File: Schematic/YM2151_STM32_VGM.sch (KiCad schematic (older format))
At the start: 32 parts, among them J1 Jack_DC+12V, J1 Micro_SD_Card, J2 USB_B, U1 BluePill_STM32F103C, U2 LTC6903, U3 LD1117, U4 LM2596S-5.0, U5 CH340G, U6 OLED_128x32_I2C, U7 YM2151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

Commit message: Schematic complete
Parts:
- added 1uF: C17, symbol CP1_Small
- added 1uF: C18, symbol CP1_Small
- added C15, C16: 1uF, symbol CP1_Small
- added C19, C20: 0.22uF, symbol C_Small
- added C21, C22: 68nF, symbol C_Small
- added C23, C24: 1000uF, symbol CP1_Small
- added J3: JACK_TRS_6PINS, symbol JACK_TRS_6PINS
- added L2, L3: 22uH, symbol L
- added SW1: PWR_SWITCH, symbol SW_SPST
- added SW2: MUTE_SWITCH, symbol SW_SPDT
- added SW3: PREV, symbol SW_Push_Dual
- added SW4: RAND, symbol SW_Push_Dual
- added SW5: NEXT, symbol SW_Push_Dual
- added SW6: LOOP, symbol SW_Push_Dual
- added SW7: SHUF, symbol SW_Push_Dual
- added U10: TPA3122D2, symbol TPA3122D2
- renumbered J1 to J2
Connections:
- net labels added: LEFT_OP_OUT, LOOP, L_OUT, NEXT, PREV, RAND, RIGHT_OP_OUT, R_OUT, SHUF
- net labels removed: LEFT_AUDIO_OUT, RIGHT_AUDIO_OUT
- wire segments 113 -> 164
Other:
- note added: "External 3.3v reg. to reduce noise from OLED+SD card\n"

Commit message: In progress of appending footprints
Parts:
- removed J1: Micro_SD_Card, symbol Micro_SD_Card
- added J1: DM3CS-SF (Micro SD Card Slot), Connector_Card:SD_TE_2041021, symbol DM3CS-SF
- D1: value 1N5824 -> SS34; footprint (none) -> Diodes:DO-214AB
- J2: footprint (none) -> Connectors:BARREL_JACK
- J3: footprint (none) -> Connectors:PJ320E_3.5mm_Jack
- J4: renamed from J2; footprint (none) -> Connectors:USB_B
- SW1, SW2: footprint (none) -> Switches:1825115-1
- SW3, SW4, SW5, SW6, SW7: footprint (none) -> Buttons_Switches_THT:SW_TH_Tactile_Omron_B3F-10xx
- U10: footprint (none) -> Housings_DIP:DIP-20_W7.62mm
- U2: footprint (none) -> Housings_SSOP:MSOP-8_3x3mm_Pitch0.65mm
- U3: footprint TO_SOT_Packages_SMD:SOT-223-3Lead_TabPin2 -> TO_SOT_Packages_THT:TO-220-3_Horizontal
- U6: footprint (none) -> CustomDisplays:128x32_OLED_I2C_Module
- U7: footprint (none) -> Housings_DIP:DIP-24_W15.24mm
- U8: footprint (none) -> Housings_DIP:DIP-16_W7.62mm
- U9: footprint (none) -> Housings_DIP:DIP-14_W7.62mm
- Y1: footprint (none) -> Crystals:Crystal_HC49-U_Vertical
- gave numbers to parts that had none: 1
- renumbered 100nF to 100nF1, 1uF to 1uF1, 1uF to 1uF2, C13 to C25
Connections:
- wire segments 164 -> 165

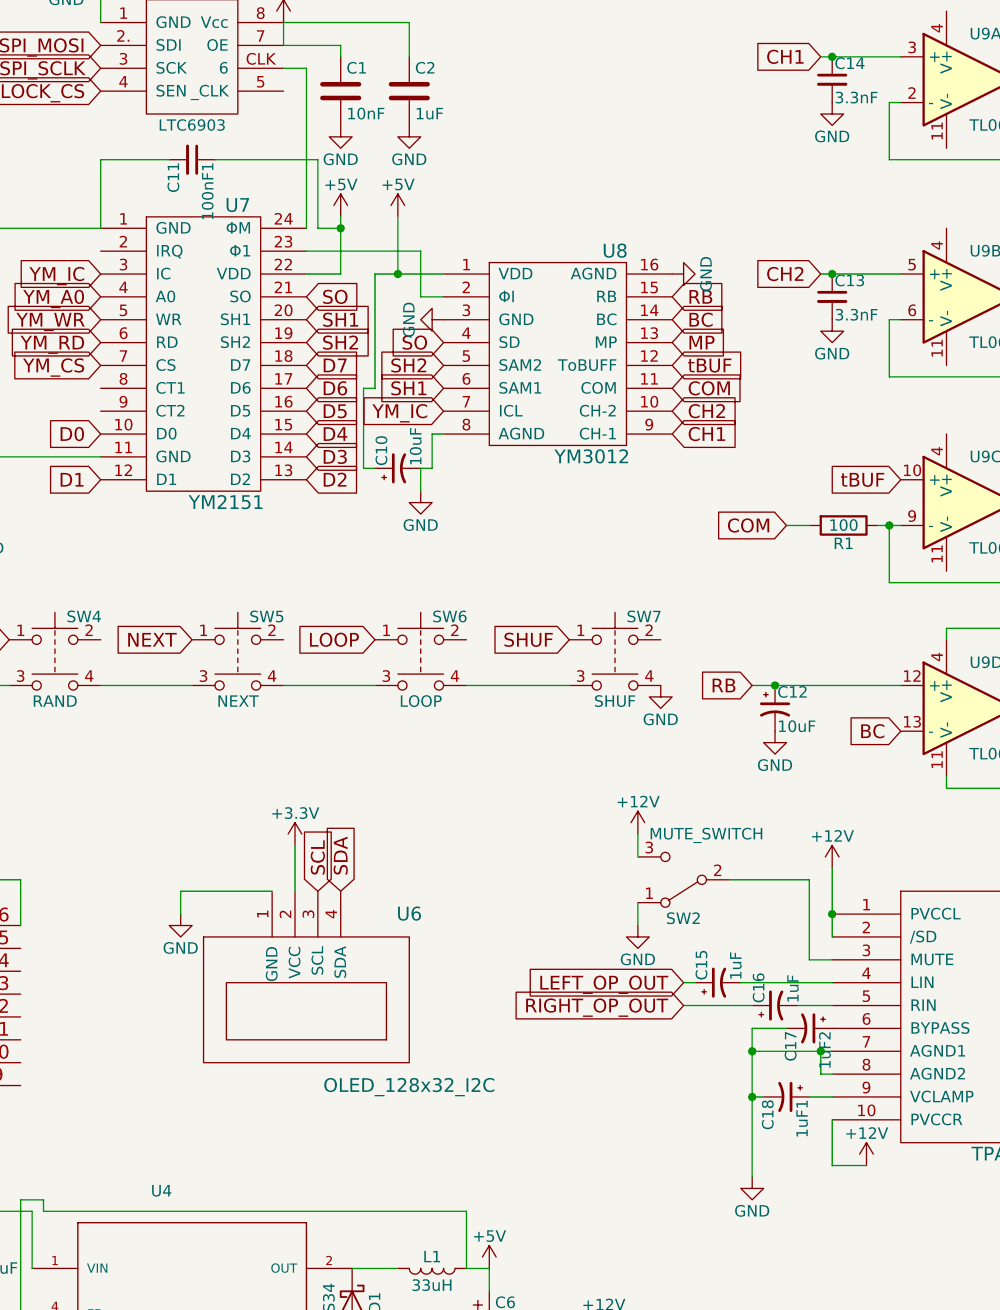
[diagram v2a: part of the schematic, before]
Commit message: Footprint selection finalized
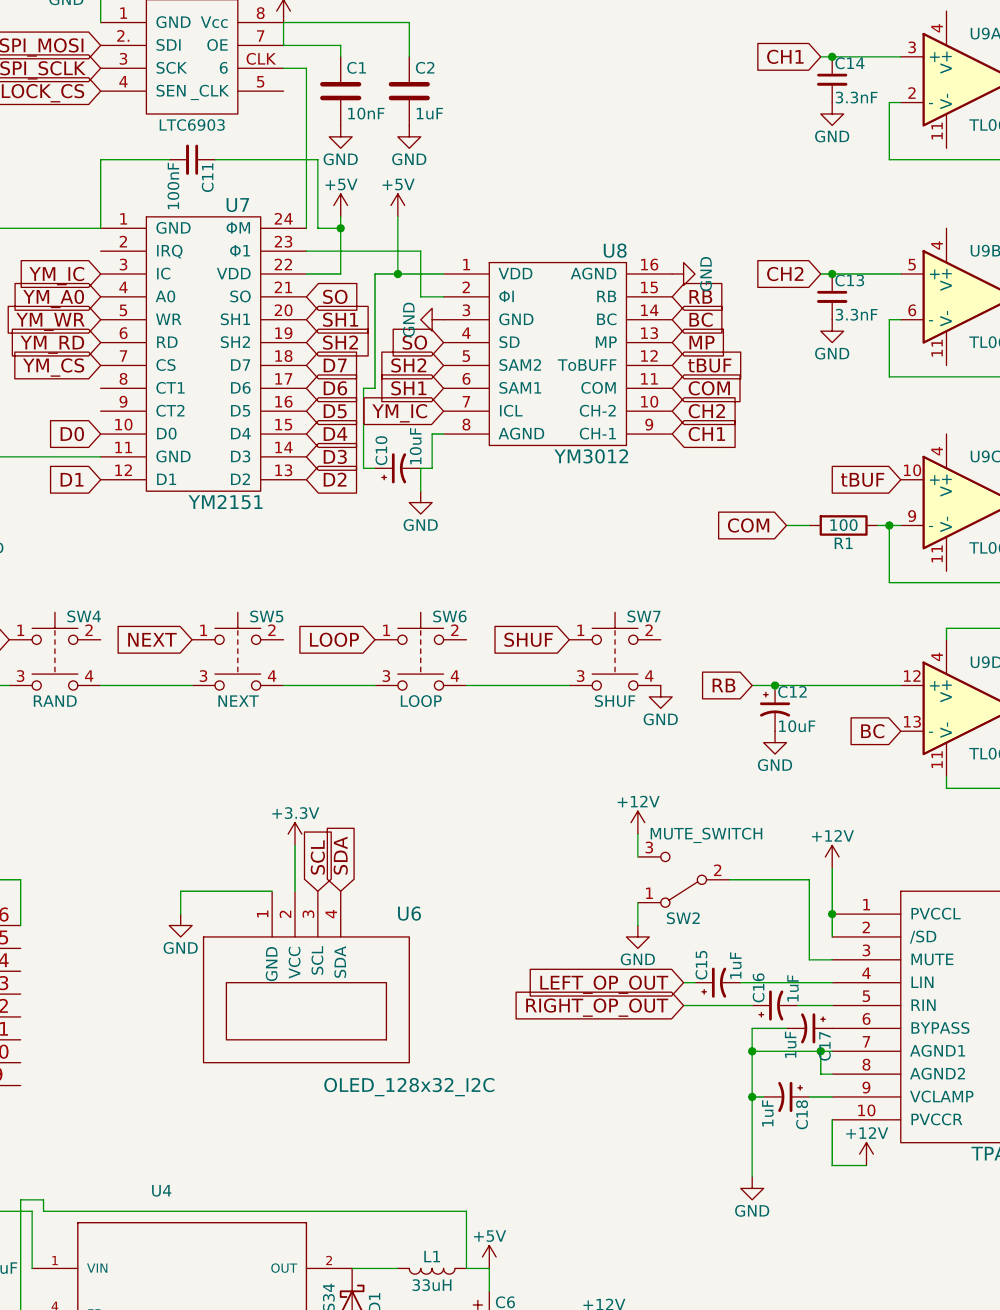
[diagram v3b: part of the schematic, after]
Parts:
- C1, C13, C14, C19, C20, C3, C7, C8: footprint (none) -> Capacitors_THT:C_Disc_D3.0mm_W1.6mm_P2.50mm
- C10, C12, C15, C16, C4: footprint (none) -> Capacitors_THT:CP_Radial_D4.0mm_P1.50mm
- C11: renamed from 100nF1; value C11 -> 100nF; footprint (none) -> Capacitors_THT:C_Disc_D3.0mm_W1.6mm_P2.50mm
- C17: renamed from 1uF2; value C17 -> 1uF; footprint (none) -> Capacitors_THT:CP_Radial_D4.0mm_P1.50mm
- C18: renamed from 1uF1; value C18 -> 1uF; footprint (none) -> Capacitors_THT:CP_Radial_D4.0mm_P1.50mm
- C2: footprint (none) -> Capacitors_THT:C_Disc_D4.7mm_W2.5mm_P5.00mm
- C21, C22: footprint (none) -> Capacitors_THT:C_Disc_D5.0mm_W2.5mm_P2.50mm
- C23, C24, C25: footprint (none) -> Capacitors_THT:CP_Radial_D8.0mm_P2.50mm
- C5: footprint (none) -> Capacitors_THT:CP_Radial_D10.0mm_P5.00mm
- C6: footprint (none) -> Capacitors_THT:CP_Radial_D6.3mm_P2.50mm
- C9: footprint 22pF -> Capacitors_THT:C_Disc_D3.0mm_W1.6mm_P2.50mm
- L1: footprint (none) -> Inductors_THT:L_Radial_D7.0mm_P3.00mm
- L2, L3: footprint (none) -> Inductors_THT:L_Radial_D8.7mm_P5.00mm_Fastron_07HCP
- R1: footprint (none) -> Resistors_THT:R_Axial_DIN0207_L6.3mm_D2.5mm_P7.62mm_Horizontal
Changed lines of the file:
@@
 F 0 "C1" H 5575 1450 50  0000 L CNN
 F 1 "10nF" H 5575 1250 50  0000 L CNN
-F 2 "" H 5588 1200 50  0001 C CNN
+F 2 "Capacitors_THT:C_Disc_D3.0mm_W1.6mm_P2.50mm" H 5588 1200 50  0001 C CNN
 F 3 "" H 5550 1350 50  0001 C CNN
 	1    5550 1350
@@
 F 0 "C2" H 5875 1450 50  0000 L CNN
 F 1 "1uF" H 5875 1250 50  0000 L CNN
-F 2 "" H 5888 1200 50  0001 C CNN
+F 2 "Capacitors_THT:C_Disc_D4.7mm_W2.5mm_P5.00mm" H 5888 1200 50  0001 C CNN
 F 3 "" H 5850 1350 50  0001 C CNN
 	1    5850 1350
@@
 F 0 "C3" H 2425 7450 50  0000 L CNN
 F 1 "100nF" H 2425 7250 50  0000 L CNN
-F 2 "" H 2438 7200 50  0001 C CNN
+F 2 "Capacitors_THT:C_Disc_D3.0mm_W1.6mm_P2.50mm" H 2438 7200 50  0001 C CNN
 F 3 "" H 2400 7350 50  0001 C CNN
 	1    2400 7350
@@
 F 0 "C4" H 3125 7450 50  0000 L CNN
 F 1 "10uF" H 3125 7250 50  0000 L CNN
-F 2 "" H 3138 7200 50  0001 C CNN
+F 2 "Capacitors_THT:CP_Radial_D4.0mm_P1.50mm" H 3138 7200 50  0001 C CNN
 F 3 "" H 3100 7350 50  0001 C CNN
 	1    3100 7350
@@
 F 0 "C5" H 3925 6500 50  0000 L CNN
 F 1 "680uF" H 3925 6300 50  0000 L CNN
-F 2 "" H 3938 6250 50  0001 C CNN
+F 2 "Capacitors_THT:CP_Radial_D10.0mm_P5.00mm" H 3938 6250 50  0001 C CNN
 F 3 "" H 3900 6400 50  0001 C CNN
 	1    3900 6400
@@
 F 0 "L1" V 5900 6500 50  0000 C CNN
 F 1 "33uH" V 6025 6500 50  0000 C CNN
-F 2 "" H 5950 6500 50  0001 C CNN
+F 2 "Inductors_THT:L_Radial_D7.0mm_P3.00mm" H 5950 6500 50  0001 C CNN
 F 3 "" H 5950 6500 50  0001 C CNN
 	1    5950 6500
@@
 F 0 "C6" H 6225 6850 50  0000 L CNN
 F 1 "220uF" H 6225 6650 50  0000 L CNN
-F 2 "" H 6238 6600 50  0001 C CNN
+F 2 "Capacitors_THT:CP_Radial_D6.3mm_P2.50mm" H 6238 6600 50  0001 C CNN
 F 3 "" H 6200 6750 50  0001 C CNN
 	1    6200 6750
@@
 F 0 "C7" H 2725 6050 50  0000 L CNN
 F 1 "100nF" H 2725 5850 50  0000 L CNN
-F 2 "" H 2738 5800 50  0001 C CNN
+F 2 "Capacitors_THT:C_Disc_D3.0mm_W1.6mm_P2.50mm" H 2738 5800 50  0001 C CNN
 F 3 "" H 2700 5950 50  0001 C CNN
 	1    2700 5950
@@
 F 0 "C9" H 2375 6450 50  0000 L CNN
 F 1 "22pF" H 2375 6250 50  0000 L CNN
-F 2 "22pF" H 2388 6200 50  0001 C CNN
+F 2 "Capacitors_THT:C_Disc_D3.0mm_W1.6mm_P2.50mm" H 2388 6200 50  0001 C CNN
 F 3 "" H 2350 6350 50  0001 C CNN
 	1    2350 6350
@@
 F 0 "C8" H 2075 6450 50  0000 L CNN
 F 1 "22pF" H 2075 6250 50  0000 L CNN
-F 2 "" H 2088 6200 50  0001 C CNN
+F 2 "Capacitors_THT:C_Disc_D3.0mm_W1.6mm_P2.50mm" H 2088 6200 50  0001 C CNN
 F 3 "" H 2050 6350 50  0001 C CNN
 	1    2050 6350
@@
 F 0 "C10" H 5810 3070 50  0000 L CNN
 F 1 "10uF" H 5810 2920 50  0000 L CNN
-F 2 "" H 5800 3000 50  0001 C CNN
+F 2 "Capacitors_THT:CP_Radial_D4.0mm_P1.50mm" H 5800 3000 50  0001 C CNN
 F 3 "" H 5800 3000 50  0001 C CNN
 	1    5800 3000
@@
 SH1
 $Comp
-L C_Small 100nF1
+L C_Small C11
 U 1 1 5A944041
 P 4900 1650
-F 0 "100nF1" H 4910 1720 50  0000 L CNN
-F 1 "C11" H 4910 1570 50  0000 L CNN
-F 2 "" H 4900 1650 50  0001 C CNN
+F 0 "C11" H 4910 1720 50  0000 L CNN
+F 1 "100nF" H 4910 1570 50  0000 L CNN
+F 2 "Capacitors_THT:C_Disc_D3.0mm_W1.6mm_P2.50mm" H 4900 1650 50  0001 C CNN
 F 3 "" H 4900 1650 50  0001 C CNN
 	1    4900 1650
@@
 F 0 "C12" H 7460 4120 50  0000 L CNN
 F 1 "10uF" H 7460 3970 50  0000 L CNN
-F 2 "" H 7450 4050 50  0001 C CNN
+F 2 "Capacitors_THT:CP_Radial_D4.0mm_P1.50mm" H 7450 4050 50  0001 C CNN
 F 3 "" H 7450 4050 50  0001 C CNN
 	1    7450 4050
@@
 F 0 "C25" H 9110 4120 50  0000 L CNN
 F 1 "1000uF" H 9110 3970 50  0000 L CNN
-F 2 "" H 9100 4050 50  0001 C CNN
+F 2 "Capacitors_THT:CP_Radial_D8.0mm_P2.50mm" H 9100 4050 50  0001 C CNN
 F 3 "" H 9100 4050 50  0001 C CNN
 	1    9100 4050
@@
 F 0 "R1" V 7830 3250 50  0000 C CNN
 F 1 "100" V 7750 3250 50  0000 C CNN
-F 2 "" V 7680 3250 50  0001 C CNN
+F 2 "Resistors_THT:R_Axial_DIN0207_L6.3mm_D2.5mm_P7.62mm_Horizontal" V 7680 3250 50  0001 C CNN
 F 3 "" H 7750 3250 50  0001 C CNN
 	1    7750 3250
@@
 F 0 "C13" H 7710 2320 50  0000 L CNN
 F 1 "3.3nF" H 7710 2170 50  0000 L CNN
-F 2 "" H 7700 2250 50  0001 C CNN
+F 2 "Capacitors_THT:C_Disc_D3.0mm_W1.6mm_P2.50mm" H 7700 2250 50  0001 C CNN
 F 3 "" H 7700 2250 50  0001 C CNN
 	1    7700 2250
@@
 F 0 "C14" H 7710 1370 50  0000 L CNN
 F 1 "3.3nF" H 7710 1220 50  0000 L CNN
-F 2 "" H 7700 1300 50  0001 C CNN
+F 2 "Capacitors_THT:C_Disc_D3.0mm_W1.6mm_P2.50mm" H 7700 1300 50  0001 C CNN
 F 3 "" H 7700 1300 50  0001 C CNN
 	1    7700 1300
@@
 F 0 "C15" H 7210 5320 50  0000 L CNN
 F 1 "1uF" H 7210 5170 50  0000 L CNN
-F 2 "" H 7200 5250 50  0001 C CNN
+F 2 "Capacitors_THT:CP_Radial_D4.0mm_P1.50mm" H 7200 5250 50  0001 C CNN
 F 3 "" H 7200 5250 50  0001 C CNN
 	1    7200 5250
@@
 F 0 "C16" H 7460 5420 50  0000 L CNN
 F 1 "1uF" H 7460 5270 50  0000 L CNN
-F 2 "" H 7450 5350 50  0001 C CNN
+F 2 "Capacitors_THT:CP_Radial_D4.0mm_P1.50mm" H 7450 5350 50  0001 C CNN
 F 3 "" H 7450 5350 50  0001 C CNN
 	1    7450 5350
@@
 $EndComp
 $Comp
-L CP1_Small 1uF2
+L CP1_Small C17
 U 1 1 5A933281
 P 7600 5450
-F 0 "1uF2" H 7610 5520 50  0000 L CNN
-F 1 "C17" H 7610 5370 50  0000 L CNN
-F 2 "" H 7600 5450 50  0001 C CNN
+F 0 "C17" H 7610 5520 50  0000 L CNN
+F 1 "1uF" H 7610 5370 50  0000 L CNN
+F 2 "Capacitors_THT:CP_Radial_D4.0mm_P1.50mm" H 7600 5450 50  0001 C CNN
 F 3 "" H 7600 5450 50  0001 C CNN
 	1    7600 5450
@@
 $EndComp
 $Comp
-L CP1_Small 1uF1
+L CP1_Small C18
 U 1 1 5A934F9E
 P 7500 5750
-F 0 "1uF1" H 7510 5820 50  0000 L CNN
-F 1 "C18" H 7510 5670 50  0000 L CNN
-F 2 "" H 7500 5750 50  0001 C CNN
+F 0 "C18" H 7510 5820 50  0000 L CNN
+F 1 "1uF" H 7510 5670 50  0000 L CNN
+F 2 "Capacitors_THT:CP_Radial_D4.0mm_P1.50mm" H 7500 5750 50  0001 C CNN
 F 3 "" H 7500 5750 50  0001 C CNN
 	1    7500 5750
@@
 F 0 "C19" H 9710 5720 50  0000 L CNN
 F 1 "0.22uF" H 9710 5570 50  0000 L CNN
-F 2 "" H 9700 5650 50  0001 C CNN
+F 2 "Capacitors_THT:C_Disc_D3.0mm_W1.6mm_P2.50mm" H 9700 5650 50  0001 C CNN
 F 3 "" H 9700 5650 50  0001 C CNN
 	1    9700 5650
@@
 F 0 "C20" H 9710 5220 50  0000 L CNN
 F 1 "0.22uF" H 9710 5070 50  0000 L CNN
-F 2 "" H 9700 5150 50  0001 C CNN
+F 2 "Capacitors_THT:C_Disc_D3.0mm_W1.6mm_P2.50mm" H 9700 5150 50  0001 C CNN
 F 3 "" H 9700 5150 50  0001 C CNN
 	1    9700 5150
@@
 F 0 "L2" V 9900 5050 50  0000 C CNN
 F 1 "22uH" V 10025 5050 50  0000 C CNN
-F 2 "" H 9950 5050 50  0001 C CNN
+F 2 "Inductors_THT:L_Radial_D8.7mm_P5.00mm_Fastron_07HCP" H 9950 5050 50  0001 C CNN
 F 3 "" H 9950 5050 50  0001 C CNN
 	1    9950 5050
@@
 F 0 "C21" H 10210 5020 50  0000 L CNN
 F 1 "68nF" H 10210 4870 50  0000 L CNN
-F 2 "" H 10200 4950 50  0001 C CNN
+F 2 "Capacitors_THT:C_Disc_D5.0mm_W2.5mm_P2.50mm" H 10200 4950 50  0001 C CNN
 F 3 "" H 10200 4950 50  0001 C CNN
 	1    10200 4950
@@
 F 0 "L3" V 9900 5750 50  0000 C CNN
 F 1 "22uH" V 10025 5750 50  0000 C CNN
-F 2 "" H 9950 5750 50  0001 C CNN
+F 2 "Inductors_THT:L_Radial_D8.7mm_P5.00mm_Fastron_07HCP" H 9950 5750 50  0001 C CNN
 F 3 "" H 9950 5750 50  0001 C CNN
 	1    9950 5750
@@
 F 0 "C22" H 10210 5920 50  0000 L CNN
 F 1 "68nF" H 10210 5770 50  0000 L CNN
-F 2 "" H 10200 5850 50  0001 C CNN
+F 2 "Capacitors_THT:C_Disc_D5.0mm_W2.5mm_P2.50mm" H 10200 5850 50  0001 C CNN
 F 3 "" H 10200 5850 50  0001 C CNN
 	1    10200 5850
@@
 F 0 "C23" H 10760 5170 50  0000 L CNN
 F 1 "1000uF" H 10760 5020 50  0000 L CNN
-F 2 "" H 10750 5100 50  0001 C CNN
+F 2 "Capacitors_THT:CP_Radial_D8.0mm_P2.50mm" H 10750 5100 50  0001 C CNN
 F 3 "" H 10750 5100 50  0001 C CNN
 	1    10750 5100
@@
 F 0 "C24" H 10760 5820 50  0000 L CNN
 F 1 "1000uF" H 10760 5670 50  0000 L CNN
-F 2 "" H 10750 5750 50  0001 C CNN
+F 2 "Capacitors_THT:CP_Radial_D8.0mm_P2.50mm" H 10750 5750 50  0001 C CNN
 F 3 "" H 10750 5750 50  0001 C CNN
 	1    10750 5750

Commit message: Finalizing PCB
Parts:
- removed U3: LD1117, TO_SOT_Packages_THT:TO-220-3_Horizontal, symbol LD1117S33TR_SOT223
- U11: footprint TO_SOT_Packages_SMD:SOT-223-3Lead_TabPin2 -> TO_SOT_Packages_SMD:SOT-223-3_TabPin2
- U4: footprint TO170P1435X465-6N -> LM2596S-5.0:TO170P1435X465-6N
- U5: footprint SOIC-16_N -> CH340G:SOIC16
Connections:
- wire segments 165 -> 171
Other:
- moved on the sheet: C2
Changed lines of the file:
@@
 U 1 1 5A920A0B
 P 4900 1200
-F 0 "U2" H 5050 1600 49  0000 C CNN
+F 0 "U2" H 5050 1500 49  0000 C CNN
 F 1 "LTC6903" H 4900 900 49  0000 C CNN
 F 2 "Housings_SSOP:MSOP-8_3x3mm_Pitch0.65mm" H 4900 1200 49  0001 C CNN
@@
 L C C2
 U 1 1 5A920E5B
-P 5850 1350
-F 0 "C2" H 5875 1450 50  0000 L CNN
-F 1 "1uF" H 5875 1250 50  0000 L CNN
-F 2 "Capacitors_THT:C_Disc_D4.7mm_W2.5mm_P5.00mm" H 5888 1200 50  0001 C CNN
-F 3 "" H 5850 1350 50  0001 C CNN
-	1    5850 1350
-	1    0    0    -1
+P 4900 750
+F 0 "C2" H 4925 850 50  0000 L CNN
+F 1 "1uF" H 4925 650 50  0000 L CNN
+F 2 "Capacitors_THT:C_Disc_D4.7mm_W2.5mm_P5.00mm" H 4938 600 50  0001 C CNN
+F 3 "" H 4900 750 50  0001 C CNN
+	1    4900 750
+	0    1    1    0
 $EndComp
 $Comp
@@
 SD_CS
 $Comp
-L LD1117S33TR_SOT223 U3
-U 1 1 5A9221FE
-P 2750 7150
-F 0 "U3" H 2600 7275 50  0000 C CNN
-F 1 "LD1117" H 2750 7275 50  0000 L CNN
-F 2 "TO_SOT_Packages_THT:TO-220-3_Horizontal" H 2750 7350 50  0001 C CNN
-F 3 "" H 2850 6900 50  0001 C CNN
-	1    2750 7150
-	1    0    0    -1
-$EndComp
-$Comp
 L GND #PWR08
 U 1 1 5A922519
@@
 F 0 "U11" H 2600 7275 50  0000 C CNN
 F 1 "LD1117" H 2750 7275 50  0000 L CNN
-F 2 "TO_SOT_Packages_SMD:SOT-223-3Lead_TabPin2" H 2750 7350 50  0001 C CNN
+F 2 "TO_SOT_Packages_SMD:SOT-223-3_TabPin2" H 2750 7350 50  0001 C CNN
 F 3 "" H 2850 6900 50  0001 C CNN
 	1    2750 7150
@@
 F 0 "U4" H 4719 7209 50  0000 L BNN
 F 1 "LM2596S-5.0" H 4800 6000 50  0000 L BNN
-F 2 "TO170P1435X465-6N" H 4900 6700 50  0001 L BNN
+F 2 "LM2596S-5.0:TO170P1435X465-6N" H 4900 6700 50  0001 L BNN
 F 3 "IC REG BUCK 5V 3A TO263-5" H 4900 6700 50  0001 L BNN
 F 4 "Texas" H 4900 6700 50  0001 L BNN "Field4"
@@
 F 0 "U5" H 3450 5960 60  0000 C CNN
 F 1 "CH340G" H 3450 4940 60  0000 C CNN
-F 2 "SOIC-16_N" H 3450 4850 40  0001 C CNN
+F 2 "CH340G:SOIC16" H 3450 4850 40  0001 C CNN
 F 3 "" H 3450 5400 60  0000 C CNN
 	1    3450 5400
@@
 Text GLabel 8900 1300 2    60   Input ~ 0
 LEFT_OP_OUT
-Text Notes 2050 6900 0    39   ~ 0
+Text Notes 2150 6900 0    39   ~ 0
 External 3.3v reg. to reduce noise from OLED+SD card\n
 $Comp
@@
 	5550 1150 5550 1200
 Wire Wire Line
-	5300 1050 5850 1050
-Wire Wire Line
-	5850 1050 5850 1200
-Wire Wire Line
 	4500 1050 4500 800
 Wire Wire Line
-	4500 800  4350 800
+	4350 800  4700 800
 Wire Wire Line
 	2750 7450 2750 7550
-Wire Wire Line
-	3050 7150 3250 7150
 Wire Wire Line
 	3100 7150 3100 7200
@@
 Connection ~ 2750 7500
 Connection ~ 2400 7150
-Connection ~ 3100 7150
 Wire Wire Line
 	4200 6800 4200 7350
@@
 Wire Wire Line
 	5350 4650 5350 4850
-Wire Wire Line
-	5300 1250 5400 1250
-Wire Wire Line
-	5400 1250 5400 1950
 Wire Wire Line
 	4500 1950 4000 1950
@@
 L DM3CS-SF J1
 U 1 1 5A9660F8
-P 1400 7400
-F 0 "J1" H 1099 8153 50  0000 L BNN
-F 1 "DM3CS-SF (Micro SD Card Slot)" H 500 6550 50  0000 L BNN
-F 2 "Connector_Card:SD_TE_2041021" H 1400 7400 50  0001 L BNN
-F 3 "Hirose" H 1400 7400 50  0001 L BNN
-F 4 "CONN MICRO SD CARD HINGED TYPE" H 1400 7400 50  0001 L BNN "Field4"
-F 5 "1.14 USD" H 1400 7400 50  0001 L BNN "Field5"
-F 6 "DM3CS-SF" H 1400 7400 50  0001 L BNN "Field6"
-F 7 "None" H 1400 7400 50  0001 L BNN "Field7"
-F 8 "Good" H 1400 7400 50  0001 L BNN "Field8"
-	1    1400 7400
+P 1350 7200
+F 0 "J1" H 1049 7953 50  0000 L BNN
+F 1 "DM3CS-SF (Micro SD Card Slot)" H 450 6350 50  0000 L BNN
+F 2 "Connector_Card:SD_TE_2041021" H 1350 7200 50  0001 L BNN
+F 3 "Hirose" H 1350 7200 50  0001 L BNN
+F 4 "CONN MICRO SD CARD HINGED TYPE" H 1350 7200 50  0001 L BNN "Field4"
+F 5 "1.14 USD" H 1350 7200 50  0001 L BNN "Field5"
+F 6 "DM3CS-SF" H 1350 7200 50  0001 L BNN "Field6"
+F 7 "None" H 1350 7200 50  0001 L BNN "Field7"
+F 8 "Good" H 1350 7200 50  0001 L BNN "Field8"
+	1    1350 7200
 	0    1    1    0
 $EndComp
@@
 L GND #PWR048
 U 1 1 5A969565
-P 700 6900
-F 0 "#PWR048" H 700 6650 50  0001 C CNN
-F 1 "GND" H 700 6750 50  0000 C CNN
-F 2 "" H 700 6900 50  0001 C CNN
-F 3 "" H 700 6900 50  0001 C CNN
-	1    700  6900
-	1    0    0    -1
-$EndComp
-Wire Wire Line
-	700  6900 700  6850
-Wire Wire Line
-	700  6850 800  6850
-Wire Wire Line
-	800  6850 800  6900
-Wire Wire Line
-	800  6900 900  6900
-Text GLabel 1100 6900 1    60   Input ~ 0
+P 650 6700
+F 0 "#PWR048" H 650 6450 50  0001 C CNN
+F 1 "GND" H 650 6550 50  0000 C CNN
+F 2 "" H 650 6700 50  0001 C CNN
+F 3 "" H 650 6700 50  0001 C CNN
+	1    650  6700
+	1    0    0    -1
+$EndComp
+Wire Wire Line
+	650  6700 650  6650
+Wire Wire Line
+	650  6650 750  6650
+Wire Wire Line
+	750  6650 750  6700
+Wire Wire Line
+	750  6700 850  6700
+Text GLabel 1050 6700 1    60   Input ~ 0
 SD_CS
-Text GLabel 1400 6900 1    60   Input ~ 0
+Text GLabel 1350 6700 1    60   Input ~ 0
 SPI_MISO
-Text GLabel 1700 6900 1    60   Input ~ 0
+Text GLabel 1650 6700 1    60   Input ~ 0
 SPI_SCLK
-Text GLabel 1800 6900 1    60   Input ~ 0
+Text GLabel 1750 6700 1    60   Input ~ 0
 SPI_MOSI
 $Comp
 L +3.3V #PWR049
 U 1 1 5A96B5CD
-P 2000 6900
-F 0 "#PWR049" H 2000 6750 50  0001 C CNN
-F 1 "+3.3V" H 2000 7040 50  0000 C CNN
-F 2 "" H 2000 6900 50  0001 C CNN
-F 3 "" H 2000 6900 50  0001 C CNN
-	1    2000 6900
-	1    0    0    -1
-$EndComp
+P 1950 6700
+F 0 "#PWR049" H 1950 6550 50  0001 C CNN
+F 1 "+3.3V" H 1950 6840 50  0000 C CNN
+F 2 "" H 1950 6700 50  0001 C CNN
+F 3 "" H 1950 6700 50  0001 C CNN
+	1    1950 6700
+	1    0    0    -1
+$EndComp
+Wire Wire Line
+	3050 7150 3250 7150
+Connection ~ 3100 7150
+$Comp
+L GND #PWR050
+U 1 1 5A938213
+P 1200 7600
+F 0 "#PWR050" H 1200 7350 50  0001 C CNN
+F 1 "GND" H 1200 7450 50  0000 C CNN
+F 2 "" H 1200 7600 50  0001 C CNN
+F 3 "" H 1200 7600 50  0001 C CNN
+	1    1200 7600
+	1    0    0    -1
+$EndComp
+Wire Wire Line
+	700  7700 1100 7700
+Connection ~ 800  7700
+Wire Wire Line
+	1100 7700 1100 7600
+Wire Wire Line
+	1100 7600 1200 7600
+Connection ~ 900  7700
+Wire Wire Line
+	5400 1250 5400 1950
+Wire Wire Line
+	5300 1250 5400 1250
+Wire Wire Line
+	4700 800  4700 750
+Wire Wire Line
+	4700 750  4750 750
+Connection ~ 4500 800
+Wire Wire Line
+	5300 1050 5450 1050
+Wire Wire Line
+	5450 1050 5450 750
+Wire Wire Line
+	5450 750  5050 750
 $EndSCHEMATC
